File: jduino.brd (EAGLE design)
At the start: 55.5 x 57.1 mm, 21 parts, among them IC1 LM2936Z-5.0, IC2 ATMEGA48/88/168-PU, J4 6V - 30V in, Q1 16 mHz

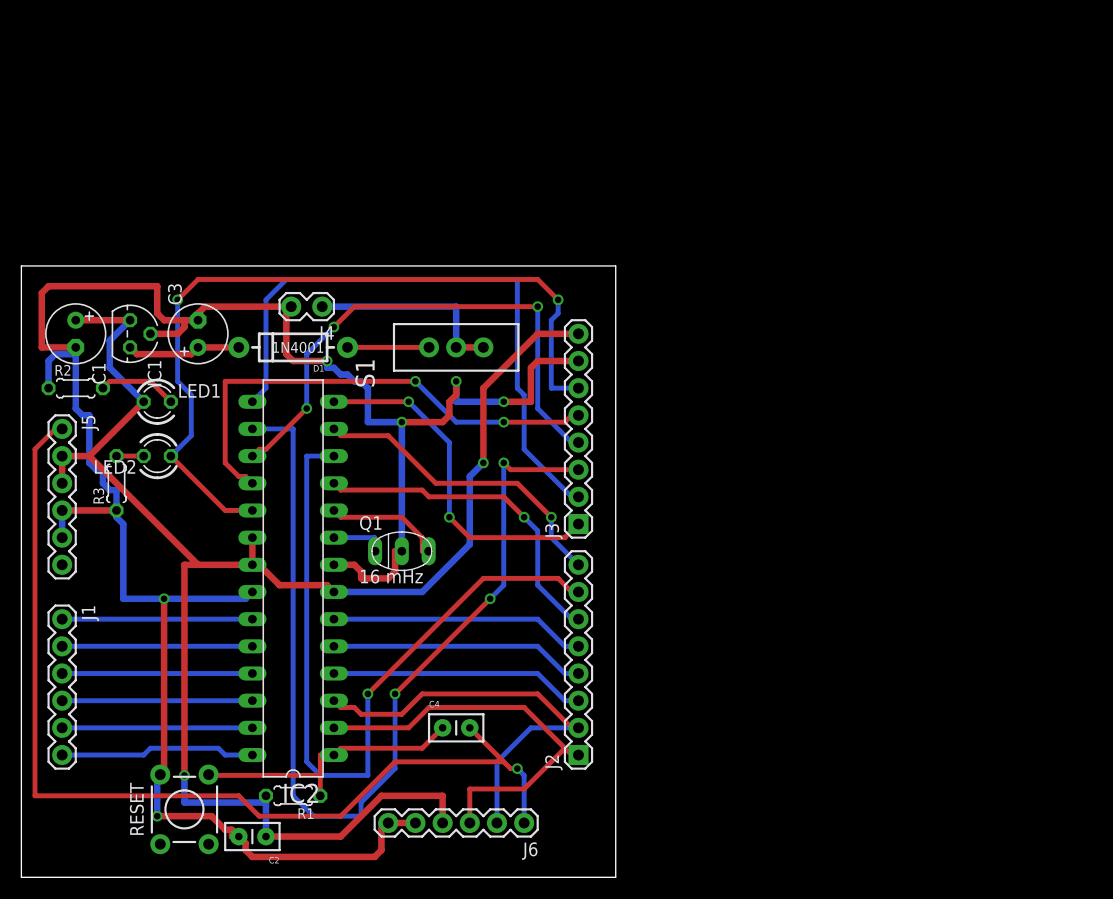
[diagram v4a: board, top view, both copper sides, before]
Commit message: Finished one-sided layout.
Completed a one-sided layout of the board that only requires three
jumpers.
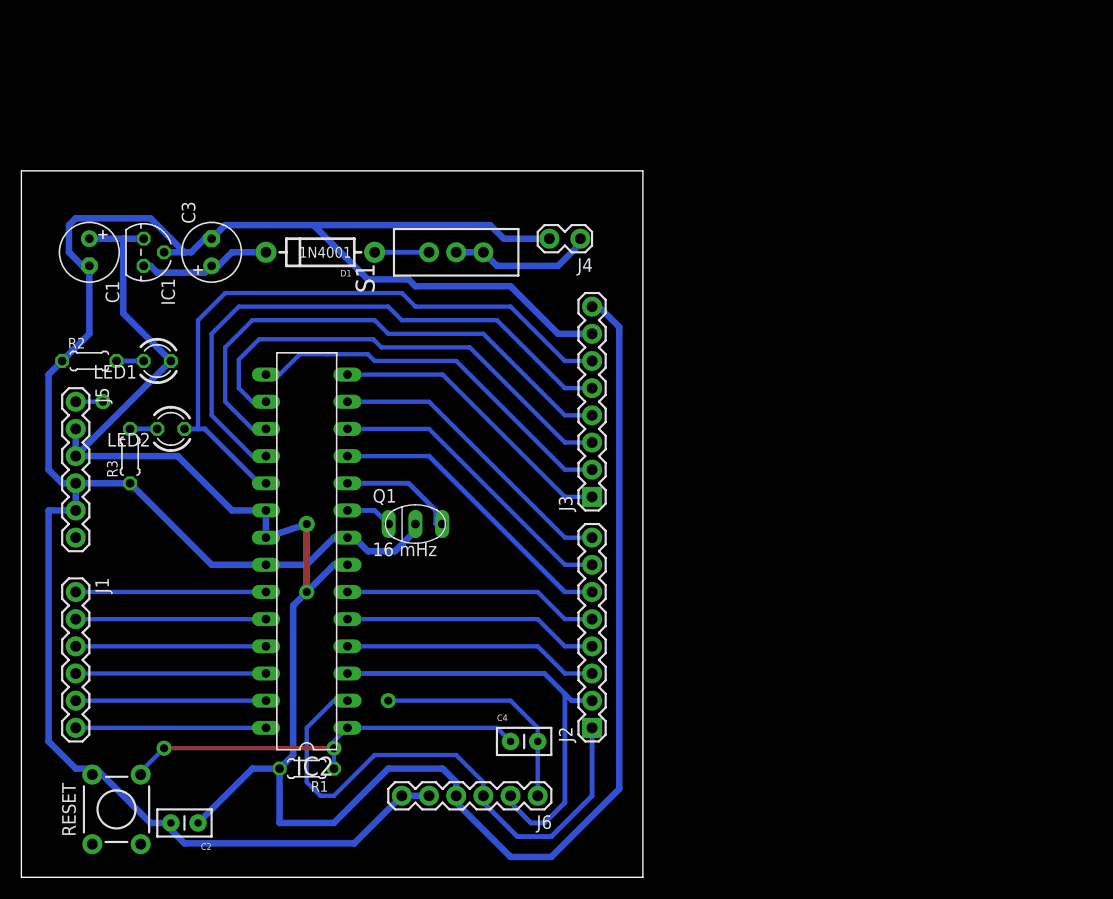
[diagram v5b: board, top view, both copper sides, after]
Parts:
- moved J4 25.0 mm to (52.1, 59.7)
- moved D1 9.25 mm to (27.9, 58.4)
- moved S1 8.89 mm to (40.6, 58.4)
- moved C1 7.73 mm to (6.35, 58.4)
- moved C3 7.73 mm to (17.8, 58.4)
- moved IC1 7.73 mm to (11.4, 58.4)
- moved C4 6.48 mm to (45.7, 12.7)
- moved C2 6.48 mm to (16.5, 5.08)
- moved RESET 6.35 mm to (8.89, 6.35)
- moved LED1 3.81 mm to (12.7, 48.3), turned to 180 degrees
- moved J5 2.84 mm to (5.08, 44.5)
- moved J1 2.84 mm to (5.08, 26.7)
- moved J2 2.84 mm to (53.3, 14.0)
- moved R1 2.84 mm to (26.7, 10.2)
- moved IC2 2.84 mm to (26.7, 30.5)
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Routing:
- net N$1: track 93.8 -> 24.5 mm, vias 1 -> 2
- net D10: track 91.0 -> 43.5 mm, vias 3 -> 0
- net D6: track 69.7 -> 28.1 mm, vias 1 -> 0
- net +5V: track 153.9 -> 191.0 mm
- net D9: track 57.4 -> 35.7 mm
- net D13: track 73.8 -> 60.4 mm, vias 2 -> 0
- net RESET: track 26.7 -> 39.3 mm, vias 0 -> 2
- net D0: track 39.1 -> 50.9 mm
- net GND: track 207.7 -> 216.1 mm, vias 6 -> 0
- net D12: track 45.8 -> 54.0 mm, vias 2 -> 0
- net N$2: track 18.9 -> 13.6 mm
- net D8: track 32.7 -> 27.6 mm, vias 2 -> 0
- net N$26: track 7.40 -> 2.54 mm
- net D5: track 31.1 -> 28.1 mm, vias 1 -> 0
- net N$7: track 7.62 -> 5.08 mm
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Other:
- board size 55.5 x 57.1 mm -> 58.1 x 66 mm

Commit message: Recentered circuit on board.
That last revisions left some traces too near the edge of the
board. Moved the circuit to have at least 0.1 inch clearance on all
board edges.
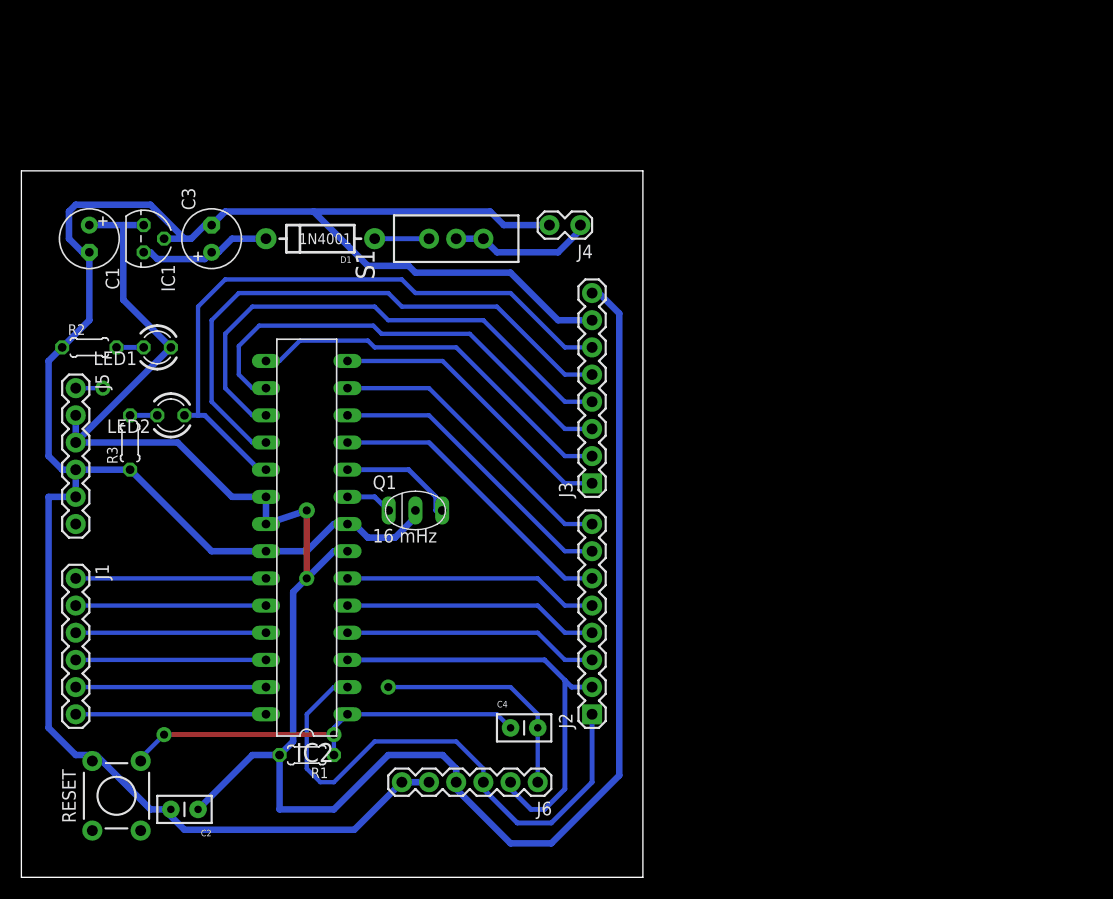
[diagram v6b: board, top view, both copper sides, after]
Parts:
- moved J4 1.27 mm to (52.1, 61.0)
- moved LED1 1.27 mm to (12.7, 49.5)
- moved LED2 1.27 mm to (14.0, 43.2)
- moved R2 1.27 mm to (6.35, 49.5)
- moved R3 1.27 mm to (10.2, 40.6)
- moved C4 1.27 mm to (45.7, 14.0)
- moved J6 1.27 mm to (48.3, 8.89)
- moved RESET 1.27 mm to (8.89, 7.62)
- moved C2 1.27 mm to (16.5, 6.35)
- moved IC2 1.27 mm to (26.7, 31.8)
- moved J1 1.27 mm to (5.08, 27.9)
- moved J2 1.27 mm to (53.3, 15.2)
- moved R1 1.27 mm to (26.7, 11.4)
- moved C1 1.27 mm to (6.35, 59.7)
- moved C3 1.27 mm to (17.8, 59.7)
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
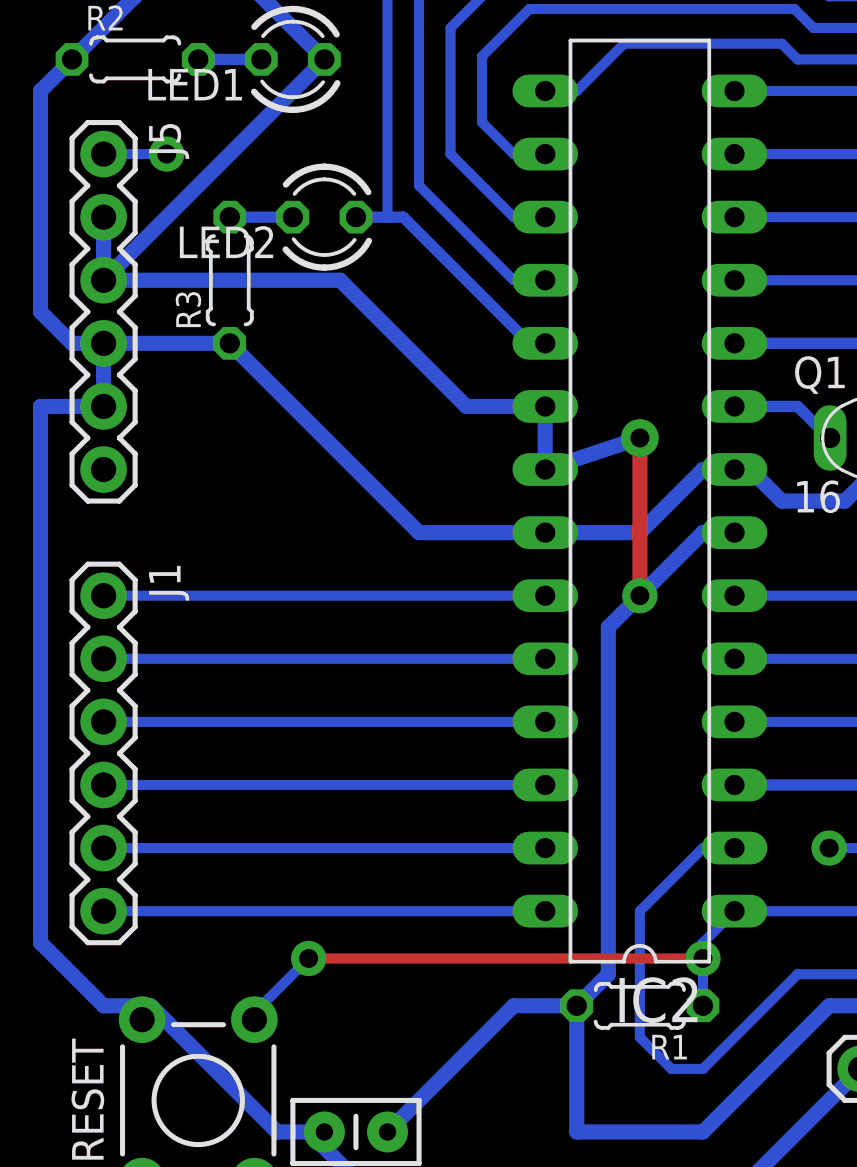
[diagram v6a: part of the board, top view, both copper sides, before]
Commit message: Reset adjustments and aesthetic improvements.
Connected reset pin on power jumper before DTR capacitor. Cleaned
up extraneous label and added a frame to the schematic.
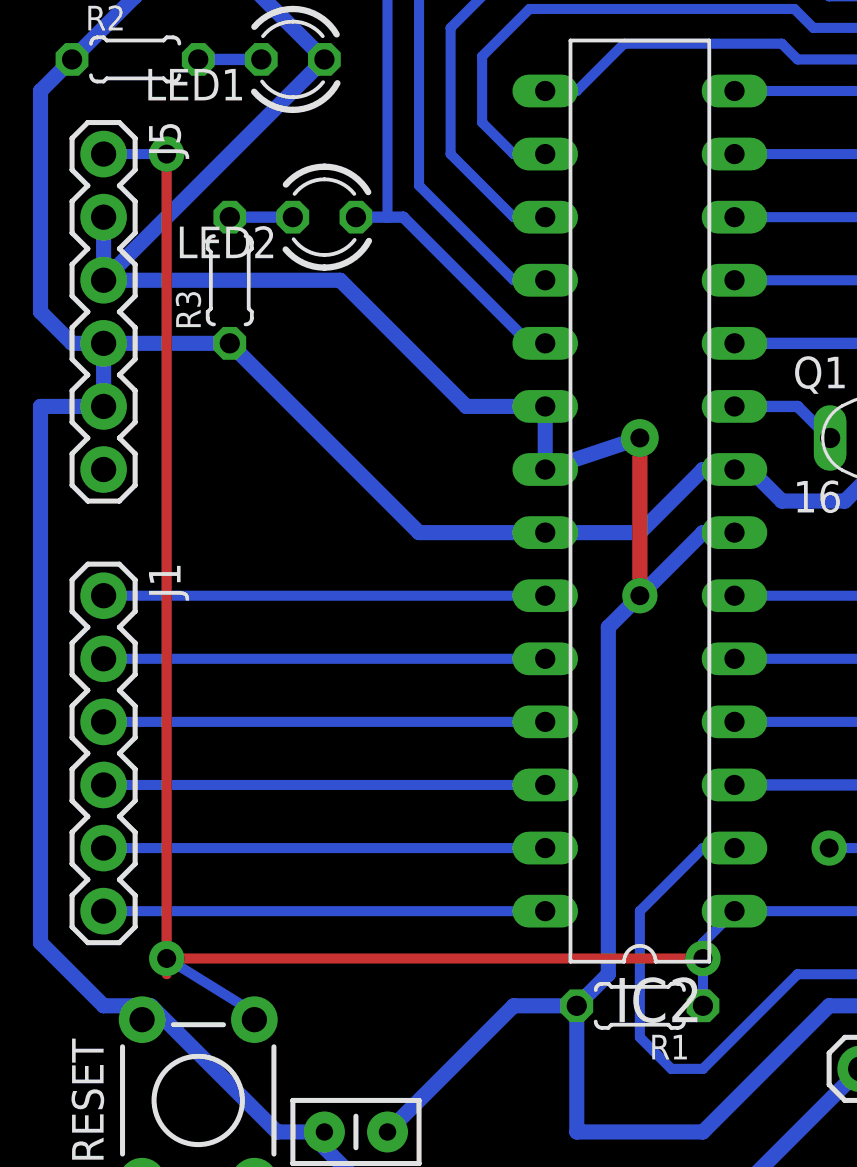
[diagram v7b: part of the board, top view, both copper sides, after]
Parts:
- J1: value (none) -> Analog I/O
- J2: value (none) -> Digital I/O
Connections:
- net N$1: no longer J5.1
- net RESET: now also J5.1
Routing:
- net RESET: track 39.3 -> 81.7 mm, vias 2 -> 3
- net N$1: track 24.5 -> 22.0 mm, vias 2 -> 1
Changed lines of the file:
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@@
 <element name="R1" library="rcl" package="0204/5" value="10K" x="26.67" y="11.43" rot="R180"/>
 <element name="Q1" library="murata-resonators" package="CSTLS_X" value="16 mHz" x="36.83" y="34.29"/>
-<element name="J1" library="SparkFun" package="1X06" value="" x="5.08" y="27.94" rot="R270"/>
-<element name="J2" library="SparkFun" package="1X08" value="" x="53.34" y="15.24" rot="R90"/>
+<element name="J1" library="SparkFun" package="1X06" value="Analog I/O" x="5.08" y="27.94" rot="R270"/>
+<element name="J2" library="SparkFun" package="1X08" value="Digital I/O" x="53.34" y="15.24" rot="R90"/>
 <element name="J4" library="SparkFun" package="1X02_LOCK" value="6V - 30V in" x="52.07" y="60.96" rot="R180"/>
 <element name="R2" library="rcl" package="0204/5" value="330" x="6.35" y="49.53"/>
@@
 <wire x1="29.21" y1="13.335" x2="29.21" y2="11.43" width="0.4064" layer="16"/>
 <wire x1="11.1506" y1="10.8712" x2="11.1506" y2="11.1506" width="0.4064" layer="16"/>
-<wire x1="11.1506" y1="11.1506" x2="13.335" y2="13.335" width="0.4064" layer="16"/>
-<wire x1="13.335" y1="13.335" x2="29.21" y2="13.335" width="0.4064" layer="1"/>
-<via x="13.335" y="13.335" extent="1-16" drill="0.762" diameter="1.4224"/>
+<wire x1="11.1506" y1="11.1506" x2="7.62" y2="13.335" width="0.4064" layer="16"/>
+<wire x1="7.62" y1="13.335" x2="29.21" y2="13.335" width="0.4064" layer="1"/>
+<via x="7.62" y="13.335" extent="1-16" drill="0.762" diameter="1.4224"/>
 <via x="29.21" y="13.335" extent="1-16" drill="0.762" diameter="1.4224"/>
+<contactref element="J5" pad="1"/>
+<wire x1="5.08" y1="45.72" x2="7.62" y2="45.72" width="0.4064" layer="16"/>
+<via x="7.62" y="45.72" extent="1-16" drill="0.762" diameter="1.4224"/>
+<wire x1="7.62" y1="45.72" x2="7.62" y2="12.7" width="0.4064" layer="1"/>
+<wire x1="7.62" y1="12.7" x2="7.62" y2="13.335" width="0" layer="19" extent="1-16"/>
 </signal>
 <signal name="A0">
@@
 <signal name="N$1">
 <contactref element="J6" pad="1"/>
-<contactref element="J5" pad="1"/>
 <contactref element="C4" pad="2"/>
 <wire x1="48.26" y1="8.89" x2="48.26" y2="9.525" width="0.4572" layer="16"/>
@@
 <wire x1="48.26" y1="15.24" x2="45.72" y2="17.78" width="0.4064" layer="16"/>
 <wire x1="45.72" y1="17.78" x2="34.29" y2="17.78" width="0.4064" layer="16"/>
-<wire x1="5.08" y1="45.72" x2="7.62" y2="45.72" width="0.4064" layer="16"/>
-<via x="7.62" y="45.72" extent="1-16" drill="0.762" diameter="1.4224"/>
 <via x="34.29" y="17.78" extent="1-16" drill="0.762" diameter="1.4224"/>
-<wire x1="34.29" y1="17.78" x2="7.62" y2="45.72" width="0" layer="19" extent="16-16"/>
 </signal>
 <signal name="N$4">

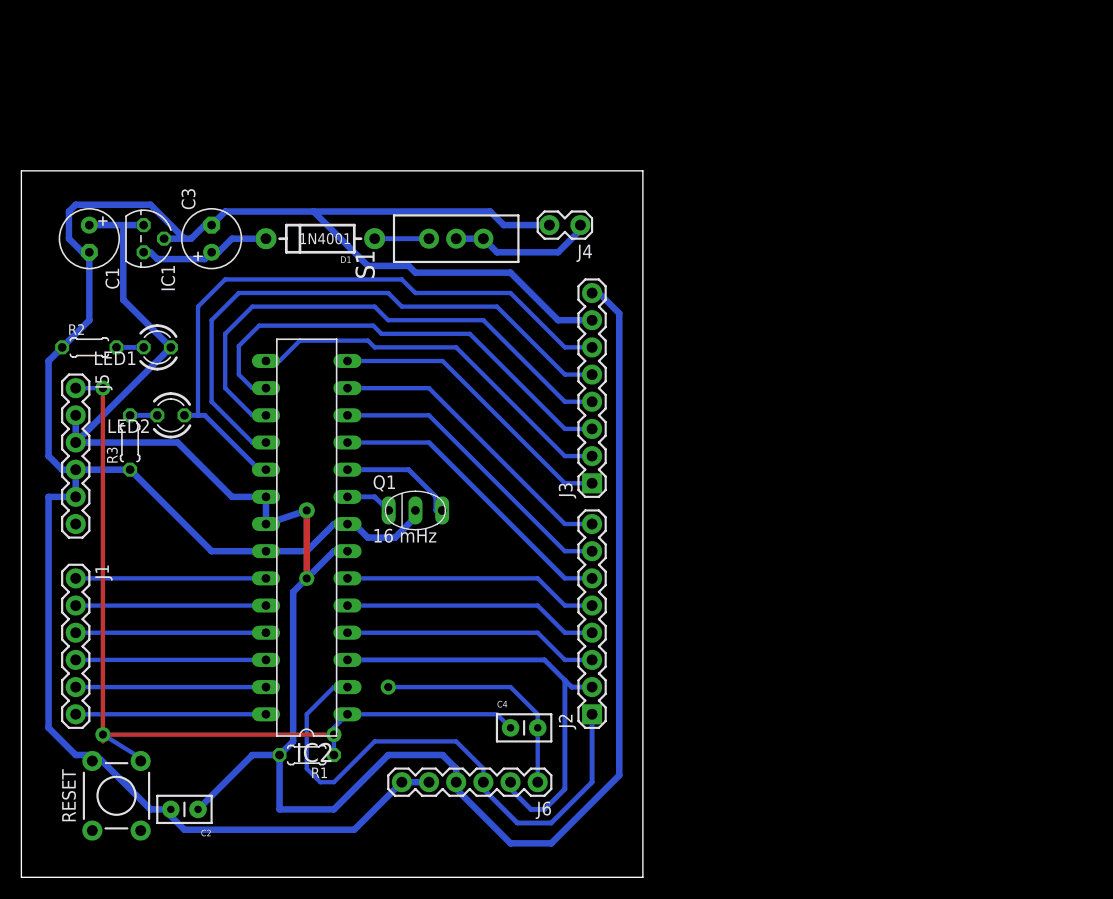
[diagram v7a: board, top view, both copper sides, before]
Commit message: Added mounting holes to the board.
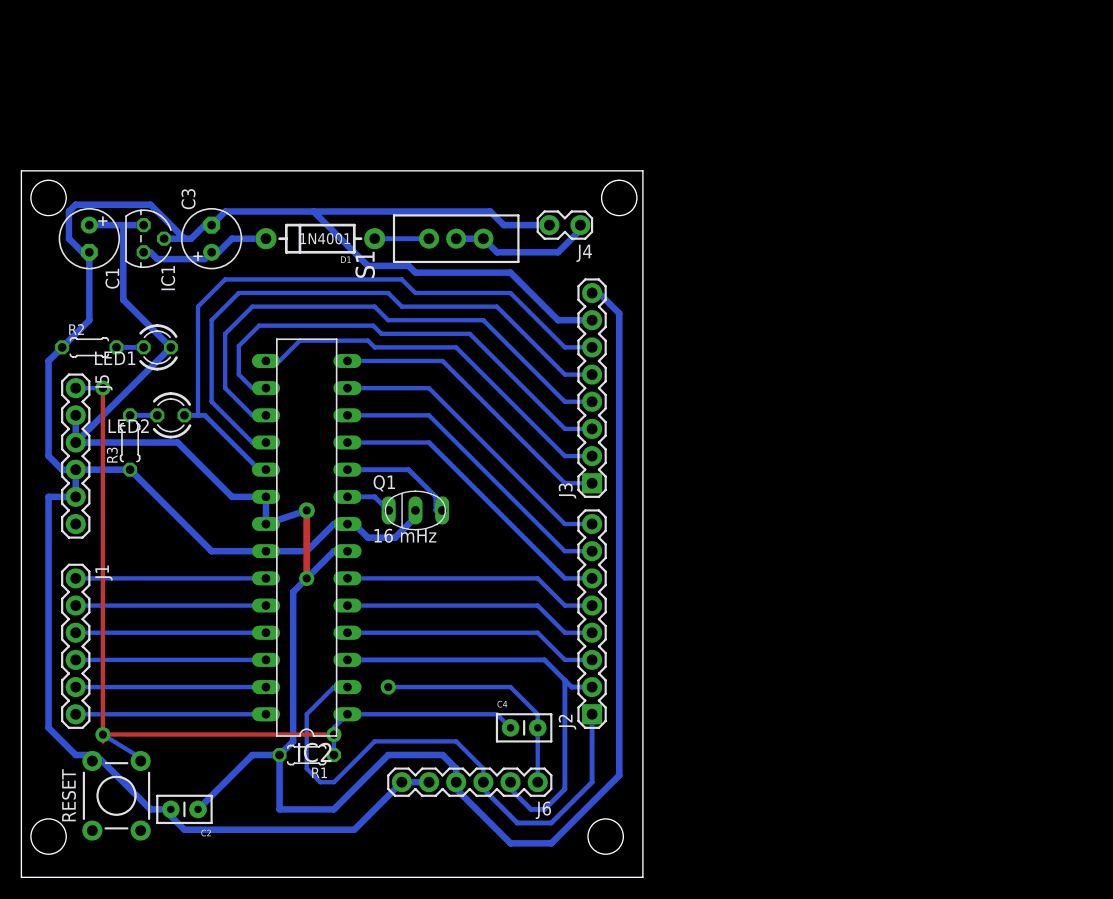
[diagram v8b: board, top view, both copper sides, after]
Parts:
- added JP1, JP2, JP3, JP4: STAND-OFF, SparkFun-Electromechanical:STAND-OFF
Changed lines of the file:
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@@
 <?xml version="1.0" encoding="utf-8"?>
 <!DOCTYPE eagle SYSTEM "eagle.dtd">
-<eagle version="6.1">
+<eagle version="6.2">
 <drawing>
 <settings>
@@
 <layer number="23" name="tOrigins" color="15" fill="1" visible="yes" active="yes"/>
 <layer number="24" name="bOrigins" color="15" fill="1" visible="yes" active="yes"/>
-<layer number="25" name="tNames" color="7" fill="1" visible="no" active="yes"/>
-<layer number="26" name="bNames" color="7" fill="1" visible="no" active="yes"/>
-<layer number="27" name="tValues" color="7" fill="1" visible="no" active="yes"/>
-<layer number="28" name="bValues" color="7" fill="1" visible="no" active="yes"/>
+<layer number="25" name="tNames" color="7" fill="1" visible="yes" active="yes"/>
+<layer number="26" name="bNames" color="7" fill="1" visible="yes" active="yes"/>
+<layer number="27" name="tValues" color="7" fill="1" visible="yes" active="yes"/>
+<layer number="28" name="bValues" color="7" fill="1" visible="yes" active="yes"/>
 <layer number="29" name="tStop" color="7" fill="3" visible="no" active="yes"/>
 <layer number="30" name="bStop" color="7" fill="6" visible="no" active="yes"/>
@@
 <layer number="49" name="Reference" color="7" fill="1" visible="no" active="yes"/>
 <layer number="50" name="dxf" color="7" fill="1" visible="no" active="yes"/>
-<layer number="51" name="tDocu" color="6" fill="1" visible="yes" active="yes"/>
+<layer number="51" name="tDocu" color="6" fill="1" visible="no" active="yes"/>
 <layer number="52" name="bDocu" color="7" fill="1" visible="no" active="yes"/>
 <layer number="53" name="tGND_GNDA" color="7" fill="9" visible="no" active="no"/>
@@
 <element name="C2" library="SparkFun-Passives" package="CAP-PTH-SMALL2" value="0.1uF" x="16.51" y="6.35" rot="R180"/>
 <element name="C4" library="SparkFun-Passives" package="CAP-PTH-SMALL2" value="0.1uF" x="45.72" y="13.97"/>
+<element name="JP1" library="SparkFun-Electromechanical" package="STAND-OFF" value="STAND-OFF" x="54.61" y="3.81"/>
+<element name="JP2" library="SparkFun-Electromechanical" package="STAND-OFF" value="STAND-OFF" x="2.54" y="63.5"/>
+<element name="JP3" library="SparkFun-Electromechanical" package="STAND-OFF" value="STAND-OFF" x="55.88" y="63.5"/>
+<element name="JP4" library="SparkFun-Electromechanical" package="STAND-OFF" value="STAND-OFF" x="2.54" y="3.81"/>
 </elements>
 <signals>
